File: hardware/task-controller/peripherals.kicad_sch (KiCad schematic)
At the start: 13 parts, among them J5 Micro_SD_Card, U6 PCF8523T, Y2 32.768kHz

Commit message: mostly done layout
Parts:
- added C24: 0.1uF, Capacitor_SMD:C_0402_1005Metric, symbol Device:C
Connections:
- net +3V3: now also C24.1
- net GND: now also C24.2
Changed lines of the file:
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@@
 	(paper "A4")
+	(junction
+		(at 83.82 87.63)
+		(diameter 0)
+		(color 0 0 0 0)
+	)
 	(junction
 		(at 60.96 64.77)
@@
 	(wire
 		(pts
+			(xy 64.77 87.63) (xy 83.82 87.63)
+		)
+		(stroke
+			(width 0)
+			(type default)
+		)
+	)
+	(wire
+		(pts
 			(xy 53.34 22.86) (xy 58.42 22.86)
 		)
@@
 	(wire
 		(pts
+			(xy 64.77 114.3) (xy 64.77 109.22)
+		)
+		(stroke
+			(width 0)
+			(type default)
+		)
+	)
+	(wire
+		(pts
 			(xy 92.71 36.83) (xy 92.71 40.64)
+		)
+		(stroke
+			(width 0)
+			(type default)
+		)
+	)
+	(wire
+		(pts
+			(xy 64.77 101.6) (xy 64.77 87.63)
 		)
 		(stroke
@@
 					(unit 1)
 				)
+			)
+		)
+	)
+	(symbol
+		(lib_id "Device:C")
+		(at 64.77 105.41 0)
+		(unit 1)
+		(exclude_from_sim no)
+		(in_bom yes)
+		(on_board yes)
+		(dnp no)
+		(fields_autoplaced yes)
+		(property "Reference" "C24"
+			(at 68.58 104.1399 0)
+			(effects
+				(font
+					(size 1.27 1.27)
+				)
+				(justify left)
+			)
+		)
+		(property "Value" "0.1uF"
+			(at 68.58 106.6799 0)
+			(effects
+				(font
+					(size 1.27 1.27)
+				)
+				(justify left)
+			)
+		)
+		(property "Footprint" "Capacitor_SMD:C_0402_1005Metric"
+			(at 65.7352 109.22 0)
+			(effects
+				(font
+					(size 1.27 1.27)
+				)
+				(hide yes)
+			)
+		)
+		(property "Datasheet" "~"
+			(at 64.77 105.41 0)
+			(effects
+				(font
+					(size 1.27 1.27)
+				)
+				(hide yes)
+			)
+		)
+		(property "Description" "Unpolarized capacitor"
+			(at 64.77 105.41 0)
+			(effects
+				(font
+					(size 1.27 1.27)
+				)
+				(hide yes)
+			)
+		)
+		(property "Cost" ""
+			(at 64.77 105.41 0)
+			(effects
+				(font
+					(size 1.27 1.27)
+				)
+				(hide yes)
+			)
+		)
+		(property "LCSC Part #" "C1525 "
+			(at 64.77 105.41 0)
+			(effects
+				(font
+					(size 1.27 1.27)
+				)
+				(hide yes)
+			)
+		)
+		(property "DK #" ""
+			(at 64.77 105.41 0)
+			(effects
+				(font
+					(size 1.27 1.27)
+				)
+				(hide yes)
+			)
+		)
+		(property "JLCPCB Rotation Offset" ""
+			(at 64.77 105.41 0)
+			(effects
+				(font
+					(size 1.27 1.27)
+				)
+				(hide yes)
+			)
+		)
+		(pin "2"
+		)
+		(pin "1"
+		)
+		(instances
+			(project "task-controller"
+				(path "/3313c311-f70a-45a8-bbf4-c9e4cbd18d5c/3aafe60e-1e23-4338-8d81-213331902af8"
+					(reference "C24")
+					(unit 1)
+				)
+			)
+		)
+	)
+	(symbol
+		(lib_id "power:GND")
+		(at 64.77 114.3 0)
+		(unit 1)
+		(exclude_from_sim no)
+		(in_bom yes)
+		(on_board yes)
+		(dnp no)
+		(fields_autoplaced yes)
+		(property "Reference" "#PWR42"
+			(at 64.77 120.65 0)
+			(effects
+				(font
+					(size 1.27 1.27)
+				)
+				(hide yes)
+			)
+		)
+		(property "Value" "GND"
+			(at 64.77 119.38 0)
+			(effects
+				(font
+					(size 1.27 1.27)
+				)
+			)
+		)
+		(property "Footprint" ""
+			(at 64.77 114.3 0)
+			(effects
+				(font
+					(size 1.27 1.27)
+				)
+				(hide yes)
+			)
+		)
+		(property "Datasheet" ""
+			(at 64.77 114.3 0)
+			(effects
+				(font
+					(size 1.27 1.27)
+				)
+				(hide yes)
+			)
+		)
+		(property "Description" "Power symbol creates a global label with name \"GND\" , ground"
+			(at 64.77 114.3 0)
+			(effects
+				(font
+					(size 1.27 1.27)
+				)
+				(hide yes)
+			)
+		)
+		(pin "1"
+		)
+		(instances
+			(project "task-controller"
+				(path "/3313c311-f70a-45a8-bbf4-c9e4cbd18d5c/3aafe60e-1e23-4338-8d81-213331902af8"
+					(reference "#PWR42")
+					(unit 1)
+				)

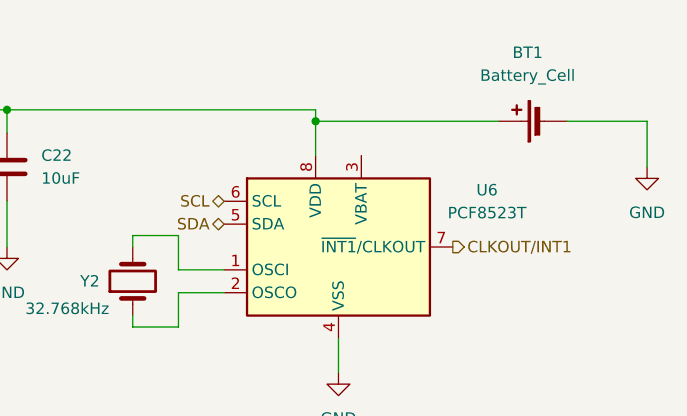
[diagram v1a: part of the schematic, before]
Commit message: changed board size
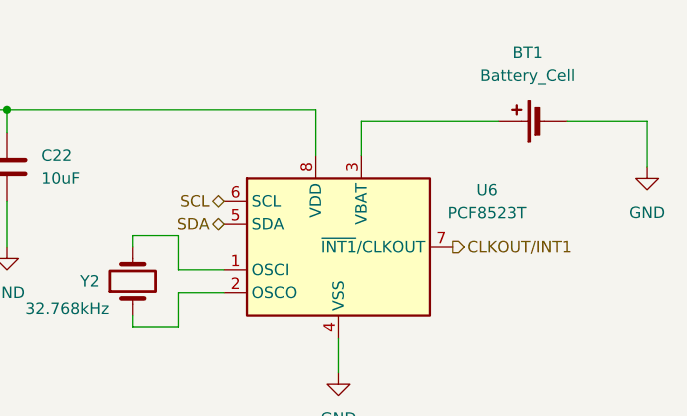
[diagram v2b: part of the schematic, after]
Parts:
- BT1: footprint (none) -> cat:XDCR-1220-006
- C22: footprint (none) -> Capacitor_SMD:C_0603_1608Metric; LCSC Part # (none) -> C19702
- Y2: footprint (none) -> Crystal:Crystal_SMD_3215-2Pin_3.2x1.5mm; LCSC Part # (none) -> C32346
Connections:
- net at C22.1, R31.1, U6.8 (VDD): no longer BT1.1 (+)
- net at U6.3 (VBAT): now also BT1.1 (+)
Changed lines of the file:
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@@
-	)
-	(junction
-		(at 107.95 24.13)
-		(diameter 0)
-		(color 0 0 0 0)
 	)
 	(junction
@@
 	(wire
 		(pts
-			(xy 128.27 24.13) (xy 107.95 24.13)
-		)
-		(stroke
-			(width 0)
-			(type default)
-		)
-	)
-	(wire
-		(pts
 			(xy 87.63 46.99) (xy 92.71 46.99)
 		)
@@
 	(wire
 		(pts
-			(xy 107.95 27.94) (xy 107.95 24.13)
+			(xy 107.95 22.86) (xy 107.95 27.94)
 		)
 		(stroke
@@
 	(wire
 		(pts
-			(xy 107.95 24.13) (xy 107.95 22.86)
-		)
-		(stroke
-			(width 0)
-			(type default)
-		)
-	)
-	(wire
-		(pts
 			(xy 83.82 101.6) (xy 83.82 92.71)
 		)
@@
 	(wire
 		(pts
+			(xy 113.03 24.13) (xy 113.03 27.94)
+		)
+		(stroke
+			(width 0)
+			(type default)
+		)
+	)
+	(wire
+		(pts
 			(xy 53.34 22.86) (xy 53.34 26.67)
 		)
@@
 		(pts
 			(xy 53.34 95.25) (xy 53.34 77.47)
+		)
+		(stroke
+			(width 0)
+			(type default)
+		)
+	)
+	(wire
+		(pts
+			(xy 128.27 24.13) (xy 113.03 24.13)
 		)
 		(stroke
@@
 			)
 		)
-		(property "Footprint" ""
+		(property "Footprint" "Capacitor_SMD:C_0603_1608Metric"
 			(at 74.6252 33.02 0)
 			(effects
@@
 		)
 		(property "Description" "Unpolarized capacitor"
+			(at 73.66 29.21 0)
+			(effects
+				(font
+					(size 1.27 1.27)
+				)
+				(hide yes)
+			)
+		)
+		(property "LCSC Part #" "C19702"
 			(at 73.66 29.21 0)
 			(effects
@@
 			)
 		)
-		(property "Footprint" ""
+		(property "Footprint" "cat:XDCR-1220-006"
 			(at 131.826 24.13 90)
 			(effects
@@
 			)
 		)
-		(property "Footprint" ""
+		(property "Footprint" "Crystal:Crystal_SMD_3215-2Pin_3.2x1.5mm"
 			(at 87.63 41.91 0)
 			(effects
@@
 			(at 87.63 41.91 0)
 			(effects
+				(font
+					(size 1.27 1.27)
+				)
+				(hide yes)
+			)
+		)
+		(property "LCSC Part #" "C32346"
+			(at 87.63 41.91 0)
+			(effects

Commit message: actual final production version
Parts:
- BT1: FT Rotation Offset (none) -> 180
- J4: renamed from J5; FT Rotation Offset (none) -> 180
- renumbered C24 to C16, C23 to C19, C22 to C20, R36 to R10, R34 to R11, R33 to R16, R32 to R18, R31 to R29, R37 to R8, R35 to R9, U6 to U5
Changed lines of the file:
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@@
 		(on_board yes)
 		(dnp no)
-		(property "Reference" "R32"
+		(property "Reference" "R18"
 			(at 71.374 73.66 90)
 			(effects
@@
 			)
 		)
-		(property "JLCPCB Rotation Offset" ""
-			(at 73.66 73.66 0)
-			(effects
-				(font
-					(size 1.27 1.27)
-				)
-				(hide yes)
-			)
-		)
 		(pin "2"
 		)
@@
 			(project "task-controller"
 				(path "/3313c311-f70a-45a8-bbf4-c9e4cbd18d5c/3aafe60e-1e23-4338-8d81-213331902af8"
-					(reference "R32")
+					(reference "R18")
 					(unit 1)
 				)
@@
 		(dnp no)
 		(fields_autoplaced yes)
-		(property "Reference" "C24"
+		(property "Reference" "C16"
 			(at 68.58 104.1399 0)
 			(effects
@@
 			)
 		)
-		(property "JLCPCB Rotation Offset" ""
-			(at 64.77 105.41 0)
-			(effects
-				(font
-					(size 1.27 1.27)
-				)
-				(hide yes)
-			)
-		)
 		(pin "2"
 		)
@@
 			(project "task-controller"
 				(path "/3313c311-f70a-45a8-bbf4-c9e4cbd18d5c/3aafe60e-1e23-4338-8d81-213331902af8"
-					(reference "C24")
+					(reference "C16")
 					(unit 1)
 				)
@@
 		(dnp no)
 		(fields_autoplaced yes)
-		(property "Reference" "C23"
+		(property "Reference" "C19"
 			(at 57.15 29.2099 0)
 			(effects
@@
 			)
 		)
-		(property "JLCPCB Rotation Offset" ""
-			(at 53.34 30.48 0)
-			(effects
-				(font
-					(size 1.27 1.27)
-				)
-				(hide yes)
-			)
-		)
 		(pin "2"
 		)
@@
 			(project "task-controller"
 				(path "/3313c311-f70a-45a8-bbf4-c9e4cbd18d5c/3aafe60e-1e23-4338-8d81-213331902af8"
-					(reference "C23")
+					(reference "C19")
 					(unit 1)
 				)
@@
 		(dnp no)
 		(fields_autoplaced yes)
-		(property "Reference" "J5"
+		(property "Reference" "J4"
 			(at 112.395 68.58 0)
 			(effects
@@
 			)
 		)
+		(property "FT Rotation Offset" "180"
+			(at 111.76 87.63 0)
+			(effects
+				(font
+					(size 1.27 1.27)
+				)
+				(hide yes)
+			)
+		)
 		(pin "6"
 		)
@@
 			(project ""
 				(path "/3313c311-f70a-45a8-bbf4-c9e4cbd18d5c/3aafe60e-1e23-4338-8d81-213331902af8"
-					(reference "J5")
+					(reference "J4")
 					(unit 1)
 				)
@@
 		(on_board yes)
 		(dnp no)
-		(property "Reference" "C22"
+		(property "Reference" "C20"
 			(at 77.47 27.9399 0)
 			(effects
@@
 			(project ""
 				(path "/3313c311-f70a-45a8-bbf4-c9e4cbd18d5c/3aafe60e-1e23-4338-8d81-213331902af8"
-					(reference "C22")
+					(reference "C20")
 					(unit 1)
 				)
@@
 			)
 		)
+		(property "FT Rotation Offset" "180"
+			(at 133.35 24.13 0)
+			(effects
+				(font
+					(size 1.27 1.27)
+				)
+				(hide yes)
+			)
+		)
 		(pin "2"
 		)
@@
 		(dnp no)
 		(fields_autoplaced yes)
-		(property "Reference" "U6"
+		(property "Reference" "U5"
 			(at 127 31.7814 0)
 			(effects
@@
 			(project ""
 				(path "/3313c311-f70a-45a8-bbf4-c9e4cbd18d5c/3aafe60e-1e23-4338-8d81-213331902af8"
-					(reference "U6")
+					(reference "U5")
 					(unit 1)
 				)
@@
 		(on_board yes)
 		(dnp no)
-		(property "Reference" "R36"
+		(property "Reference" "R10"
 			(at 51.054 73.66 90)
 			(effects
@@
 			)
 		)
-		(property "JLCPCB Rotation Offset" ""
-			(at 53.34 73.66 0)
-			(effects
-				(font
-					(size 1.27 1.27)
-				)
-				(hide yes)
-			)
-		)
 		(pin "2"
 		)
@@
 			(project "task-controller"
 				(path "/3313c311-f70a-45a8-bbf4-c9e4cbd18d5c/3aafe60e-1e23-4338-8d81-213331902af8"
-					(reference "R36")
+					(reference "R10")
 					(unit 1)
 				)
@@
 		(on_board yes)
 		(dnp no)
-		(property "Reference" "R31"
+		(property "Reference" "R29"
 			(at 62.23 25.654 90)
 			(effects
@@
 			)
 		)
-		(property "JLCPCB Rotation Offset" ""
-			(at 62.23 22.86 0)
-			(effects
-				(font
-					(size 1.27 1.27)
-				)
-				(hide yes)
-			)
-		)
 		(pin "2"
 		)
@@
 			(project "task-controller"
 				(path "/3313c311-f70a-45a8-bbf4-c9e4cbd18d5c/3aafe60e-1e23-4338-8d81-213331902af8"
-					(reference "R31")
+					(reference "R29")
 					(unit 1)
 				)
@@
 		(on_board yes)
 		(dnp no)
-		(property "Reference" "R37"
+		(property "Reference" "R8"
 			(at 45.974 73.66 90)
 			(effects
@@
 			)
 		)
-		(property "JLCPCB Rotation Offset" ""
-			(at 48.26 73.66 0)
-			(effects
-				(font
-					(size 1.27 1.27)
-				)
-				(hide yes)
-			)
-		)
 		(pin "2"
 		)
@@
 			(project "task-controller"
 				(path "/3313c311-f70a-45a8-bbf4-c9e4cbd18d5c/3aafe60e-1e23-4338-8d81-213331902af8"
-					(reference "R37")
+					(reference "R8")
 					(unit 1)
 				)
@@
 		(on_board yes)
 		(dnp no)
-		(property "Reference" "R33"
+		(property "Reference" "R16"
 			(at 66.294 73.66 90)
 			(effects
@@
 			)
 		)
-		(property "JLCPCB Rotation Offset" ""
-			(at 68.58 73.66 0)
-			(effects
-				(font
-					(size 1.27 1.27)
-				)
-				(hide yes)
-			)
-		)
 		(pin "2"
 		)
@@
 			(project "task-controller"
 				(path "/3313c311-f70a-45a8-bbf4-c9e4cbd18d5c/3aafe60e-1e23-4338-8d81-213331902af8"
-					(reference "R33")
+					(reference "R16")
 					(unit 1)
 				)
@@
 		(on_board yes)
 		(dnp no)
-		(property "Reference" "R34"
+		(property "Reference" "R11"
 			(at 61.214 73.66 90)
 			(effects
@@
 			)
 		)
-		(property "JLCPCB Rotation Offset" ""
-			(at 63.5 73.66 0)
-			(effects
-				(font
-					(size 1.27 1.27)
-				)
-				(hide yes)
-			)
-		)
 		(pin "2"
 		)
@@
 			(project "task-controller"
 				(path "/3313c311-f70a-45a8-bbf4-c9e4cbd18d5c/3aafe60e-1e23-4338-8d81-213331902af8"
-					(reference "R34")
+					(reference "R11")
 					(unit 1)
 				)
@@
 		(on_board yes)
 		(dnp no)
-		(property "Reference" "R35"
+		(property "Reference" "R9"
 			(at 56.134 73.66 90)
 			(effects
@@
 			)
 		)
-		(property "JLCPCB Rotation Offset" ""
-			(at 58.42 73.66 0)
-			(effects
-				(font
-					(size 1.27 1.27)
-				)
-				(hide yes)
-			)
-		)
 		(pin "2"
 		)
@@
 			(project "task-controller"
 				(path "/3313c311-f70a-45a8-bbf4-c9e4cbd18d5c/3aafe60e-1e23-4338-8d81-213331902af8"
-					(reference "R35")
-					(unit 1)
-				)
+					(reference "R9")
+					(unit 1)
+				)
